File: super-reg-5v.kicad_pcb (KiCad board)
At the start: 2 copper layers, 80 x 32.8 mm, 39 parts, among them Q1 2SA1015, Q2 D44H11, U1 LM317T, U2 AD825, X1 AC_IN, X2 DC_OUT

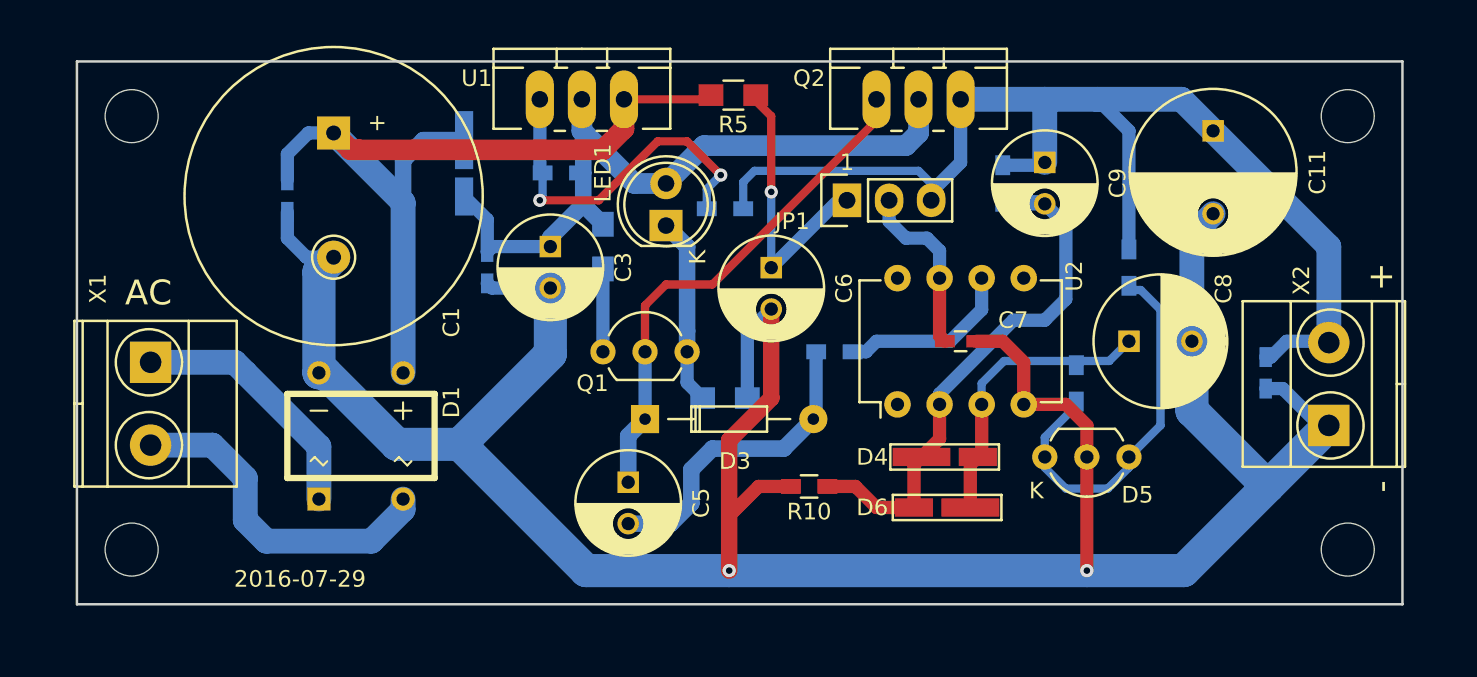
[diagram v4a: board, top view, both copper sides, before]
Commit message: change footprint for the diode add an alternate op-amp footprint
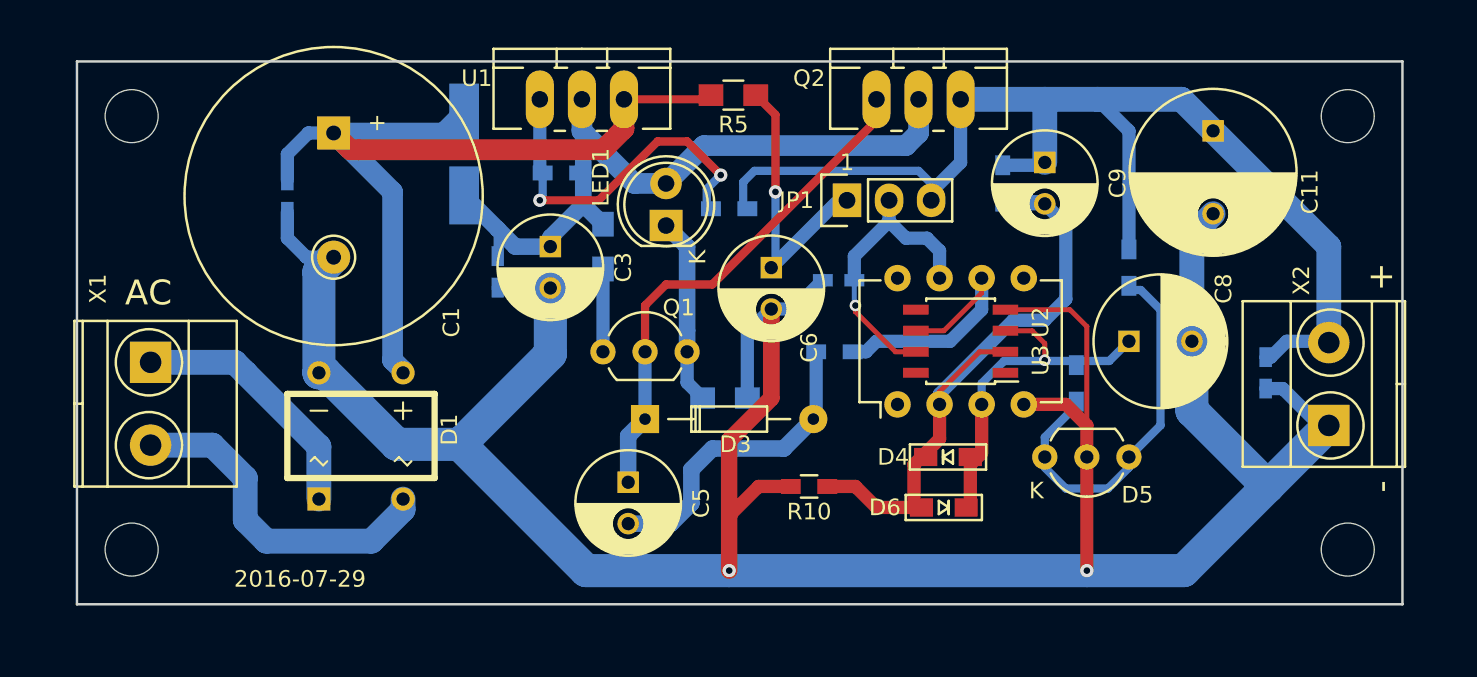
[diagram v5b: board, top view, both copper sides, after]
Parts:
- added U3: AD825, Housings_SOIC:SOIC-8_3.9x4.9mm_Pitch1.27mm, F.Cu at (168.9, 90.8)
- C11: value 470u -> 220u OS-CON
- C3, C6: value 100u -> 100u 35v LowESR
- C5: value 100u -> 100u LowESR
- C7: moved to B.Cu
- C8: value 100u -> 100u EP-Cap
- D2: footprint myfootprint:TUMD2-handsoldering -> Diodes_SMD:SMA_Handsoldering
- D3: value 2.7V -> ZD 2.7V
- D4, D6: footprint myfootprint:TUMD2-handsoldering -> myfootprint:UMD2-handsoldering
- LED1: value LED -> LED GREEN(2V)
- R8: value 1k -> 2.2k
- moved C7 8.24 mm to (161.5, 87.1), turned to 180 degrees
- moved D2 0.76 mm to (138.9, 79.5)
- moved C4 0.68 mm to (141.0, 86.6)
- moved R2 0.25 mm to (154.9, 82.8)
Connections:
- net Net-(C7-Pad1) renamed /OPAMP_PW
- net Net-(C8-Pad1) renamed /OPAMP_P
- net Net-(C9-Pad2) renamed /OPAMP_N
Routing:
- net GND: track 169.9 -> 178.4 mm
- net /OPAMP_PW: track 11.2 -> 18.2 mm, vias 0 -> 1
- net Net-(R6-Pad1): track 10.5 -> 16.3 mm
- net /OPAMP_N: track 34.7 -> 40.4 mm
- net /OPAMP_P: track 17.7 -> 21.6 mm, vias 0 -> 1
- net Net-(C1-Pad1): track 53.7 -> 55.1 mm
- net Net-(C3-Pad1): track 44.2 -> 45.1 mm
- net Net-(C6-Pad1): track 17.3 -> 17.8 mm

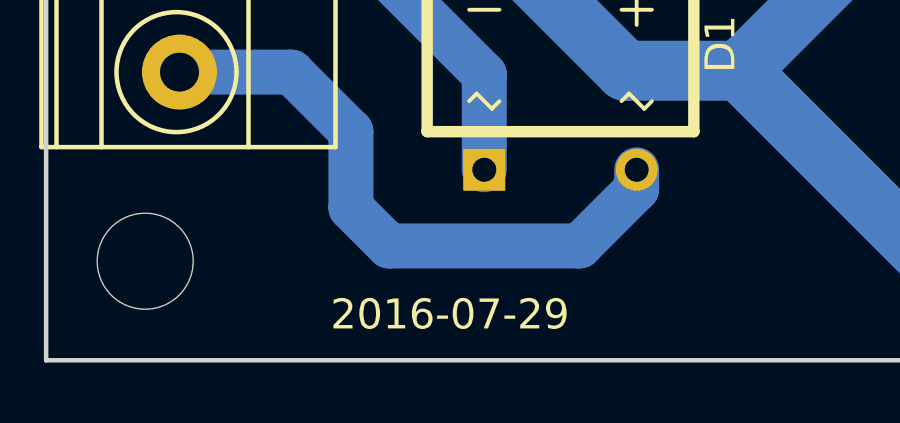
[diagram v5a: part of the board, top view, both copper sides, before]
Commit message: change the date on the board
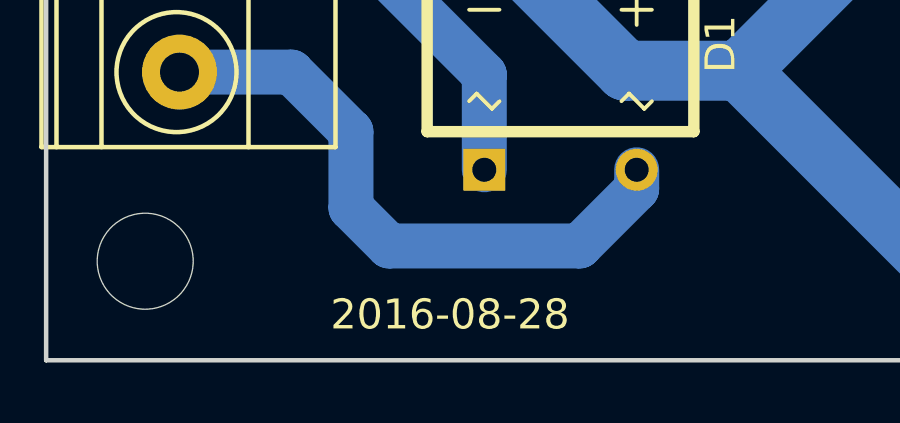
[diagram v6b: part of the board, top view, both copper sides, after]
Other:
- board text added: "2016-08-28"
- board text removed: "2016-07-29"
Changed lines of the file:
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@@
     (links 68)
     (no_connects 0)
-    (area 115.494999 73.838999 195.655001 106.755001)
+    (area 106.014857 69.056 205.135143 110.118)
     (thickness 1.6)
     (drawings 10)
@@
   )
   (setup
-    (last_trace_width 0.5)
+    (last_trace_width 0.25)
     (user_trace_width 0.25)
     (user_trace_width 0.3)
@@
     )
   )
-  (gr_text 2016-07-29 (at 129.032 105.156) (layer F.SilkS)
+  (gr_text "2016-08-28\n" (at 129.032 105.156) (layer F.SilkS)
     (effects (font (size 1 1) (thickness 0.25)))
   )
@@
   (segment (start 152.654 100.584) (end 152.654 98.552) (width 1) (layer B.Cu) (net 4))
   (segment (start 151.424 101.814) (end 152.654 100.584) (width 1) (layer B.Cu) (net 4))
-  (segment (start 157.734 86.106) (end 157.734 81.788) (width 0.5) (layer B.Cu) (net 5) (status 400000))
+  (segment (start 157.734 86.106) (end 157.734 81.788) (width 0.5) (layer B.Cu) (net 5))
   (via (at 157.734 81.788) (size 0.8) (drill 0.4) (layers F.Cu B.Cu) (net 5))
   (segment (start 157.734 77.136) (end 156.544 75.946) (width 0.5) (layer F.Cu) (net 5))
   (segment (start 157.734 81.788) (end 157.734 77.136) (width 0.5) (layer F.Cu) (net 5))
-  (segment (start 157.734 86.106) (end 157.48 86.36) (width 0.5) (layer B.Cu) (net 5) (status C00000))
+  (segment (start 157.734 86.106) (end 157.48 86.36) (width 0.5) (layer B.Cu) (net 5))
   (segment (start 156.544 76.28) (end 156.544 75.946) (width 0.5) (layer F.Cu) (net 5))
   (segment (start 162.052 81.788) (end 157.48 86.36) (width 0.8) (layer B.Cu) (net 5))

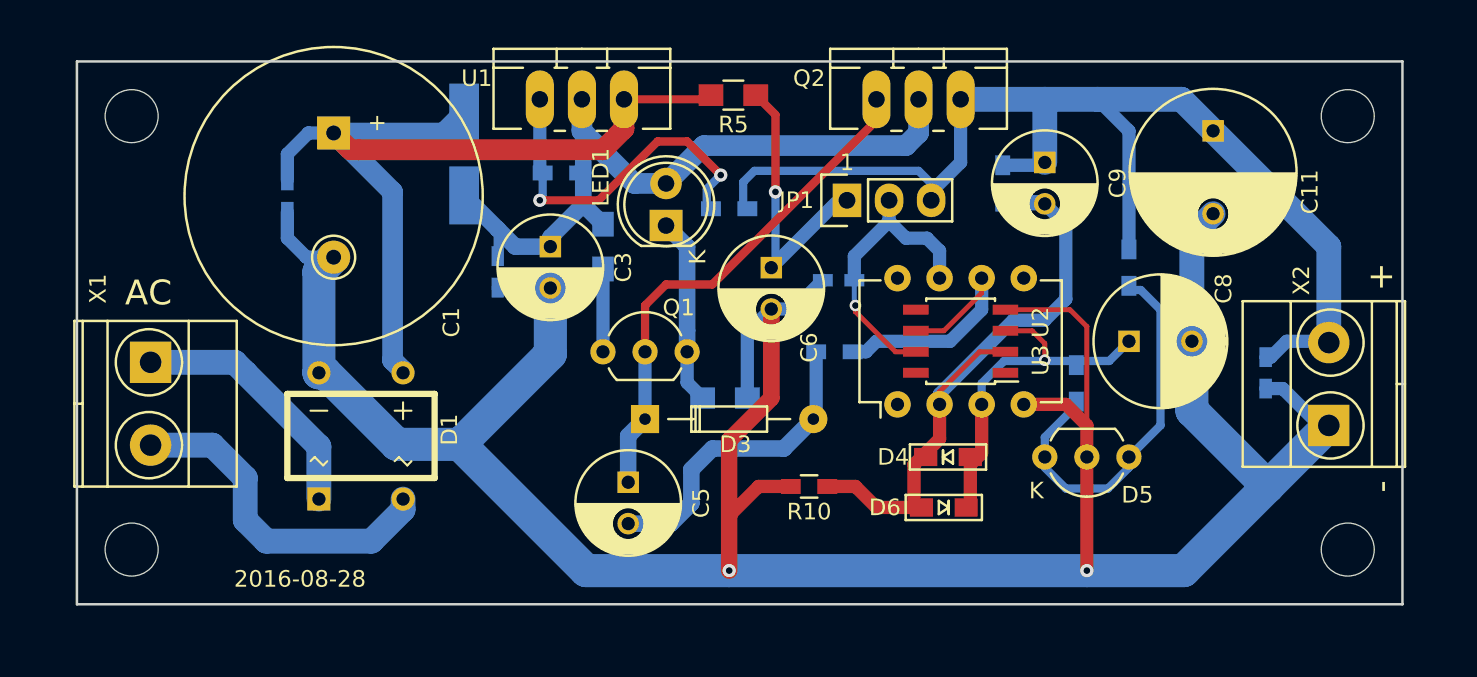
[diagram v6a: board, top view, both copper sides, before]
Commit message: change PCB size (35mm x 85mm) add alternate C1
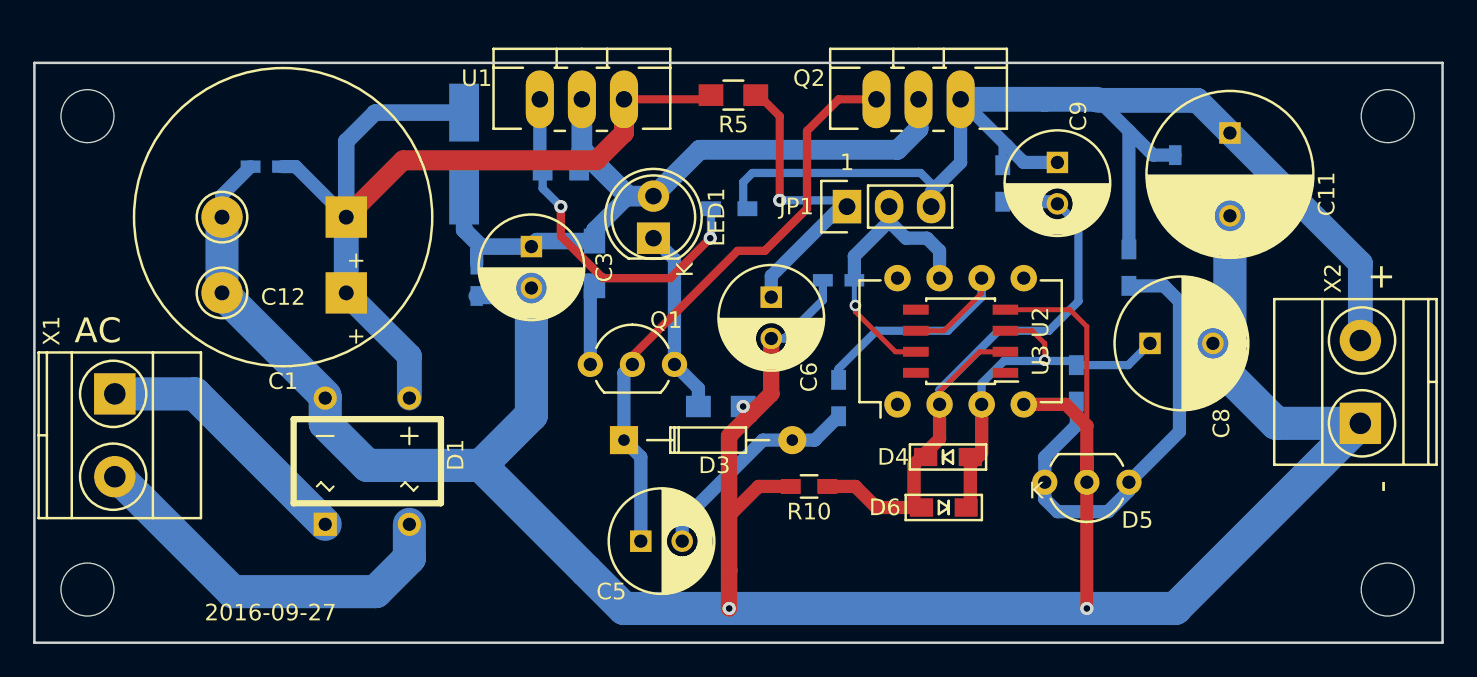
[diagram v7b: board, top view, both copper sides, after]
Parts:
- added C12: C1-Alt, myfootprint:C_Radial_D18_L36_P7.5_LargePad_NoCircle, F.Cu at (131.8, 87.9)
- moved C10 13.4 mm to (181.9, 80.5)
- moved C1 5.14 mm to (131.8, 83.3), turned to 180 degrees
- moved C5 3.64 mm to (149.6, 102.9), turned to 0 degrees
- moved REF** 3.60 mm to (116.2, 105.8)
- moved REF** 3.41 mm to (194.7, 105.8)
- moved X1 2.88 mm to (117.9, 94.0)
- moved R6 2.81 mm to (161.5, 94.2), turned to 270 degrees
- moved REF** 2.67 mm to (116.2, 77.2)
- moved ? 2.41 mm to (194.7, 77.2)
- moved C2 2.18 mm to (127.0, 80.3), turned to 180 degrees
- moved X2 1.91 mm to (193.0, 95.8)
- moved D3 1.80 mm to (148.6, 96.8)
- moved C6 1.78 mm to (157.5, 88.1)
- moved D1 1.57 mm to (133.1, 98.0)
- moved D5 1.52 mm to (179.1, 99.3)
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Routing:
- net GND: track 178.4 -> 188.9 mm, vias 2 -> 3
- net Net-(C5-Pad1): track 31.0 -> 37.0 mm
- net Net-(C5-Pad2): track 19.1 -> 13.3 mm
- net Net-(D5-Pad1): track 23.4 -> 28.7 mm
- net Net-(C10-Pad1): track 72.4 -> 76.0 mm
- net Net-(D1-Pad2): track 20.6 -> 23.5 mm
- net /OPAMP_PW: track 18.2 -> 16.4 mm
- net Net-(R6-Pad1): track 16.3 -> 18.1 mm
- net Net-(C6-Pad1): track 17.8 -> 19.2 mm
- net /OPAMP_P: track 21.6 -> 22.9 mm
- net Net-(C1-Pad1): track 55.1 -> 56.3 mm
- net /OPAMP_N: track 40.4 -> 39.8 mm
- net Net-(D1-Pad1): track 15.4 -> 16.0 mm
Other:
- board size 80 x 32.8 mm -> 85 x 35 mm
- board text added: "2016-09-27"
- board text removed: "2016-08-28"

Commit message: add alternate bridge diode
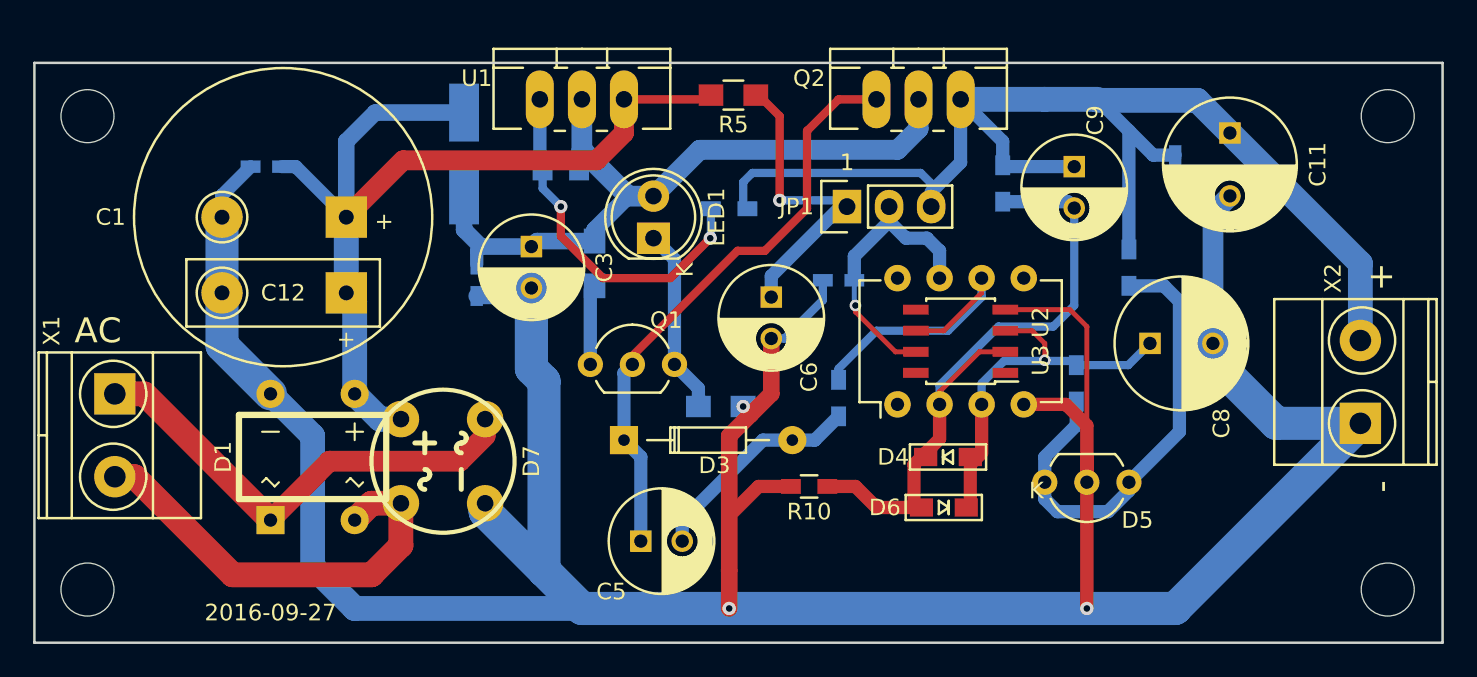
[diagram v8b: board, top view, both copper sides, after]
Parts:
- added D7: AlterBridgeD, w_pth_diodes:bridge_wob_alter_pin, F.Cu at (137.7, 98.0)
- C11: footprint Capacitors_ThroughHole:C_Radial_D10_L20_P5 -> Capacitors_ThroughHole:C_Radial_D8_L13_P3.8
- moved D1 3.31 mm to (129.8, 97.8)
- moved C9 1.05 mm to (175.8, 80.3)
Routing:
- net GND: track 188.9 -> 208.7 mm
- net Net-(D1-Pad1): track 16.0 -> 28.6 mm
- net Net-(D1-Pad2): track 23.5 -> 26.4 mm
- net Net-(C1-Pad1): track 56.3 -> 58.1 mm
